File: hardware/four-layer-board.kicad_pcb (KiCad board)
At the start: 4 copper layers, 50 x 50 mm, 65 parts, among them J1 USB_B_Micro, J2 SWD Connector, J3 PWR, J4 Conn_01x06, J5 Conn_01x06, Q1 AO3401A, SW1 B3U-1000P, U1 STM32F103C8T6, U2 AMS1117-3.3, U3 USBLC6-2SC6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

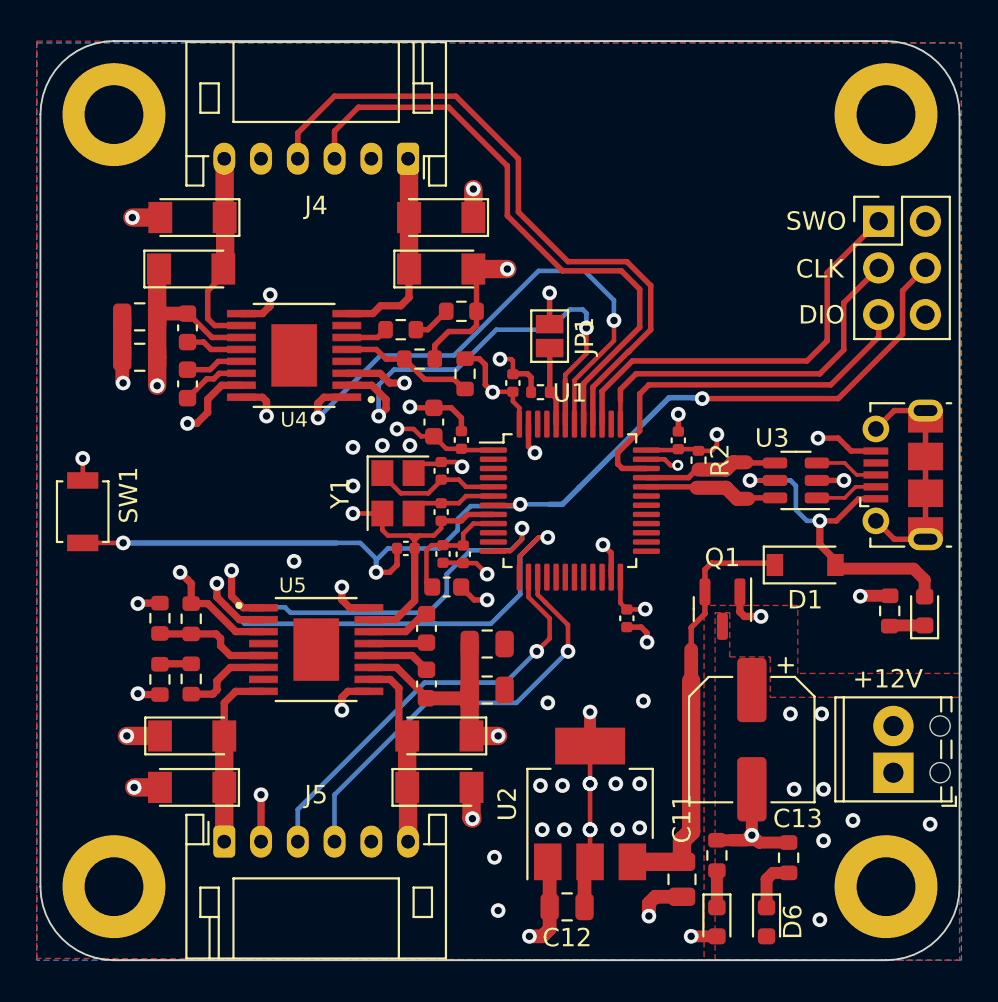
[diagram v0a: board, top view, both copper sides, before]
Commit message: Moved hardware to separate directory
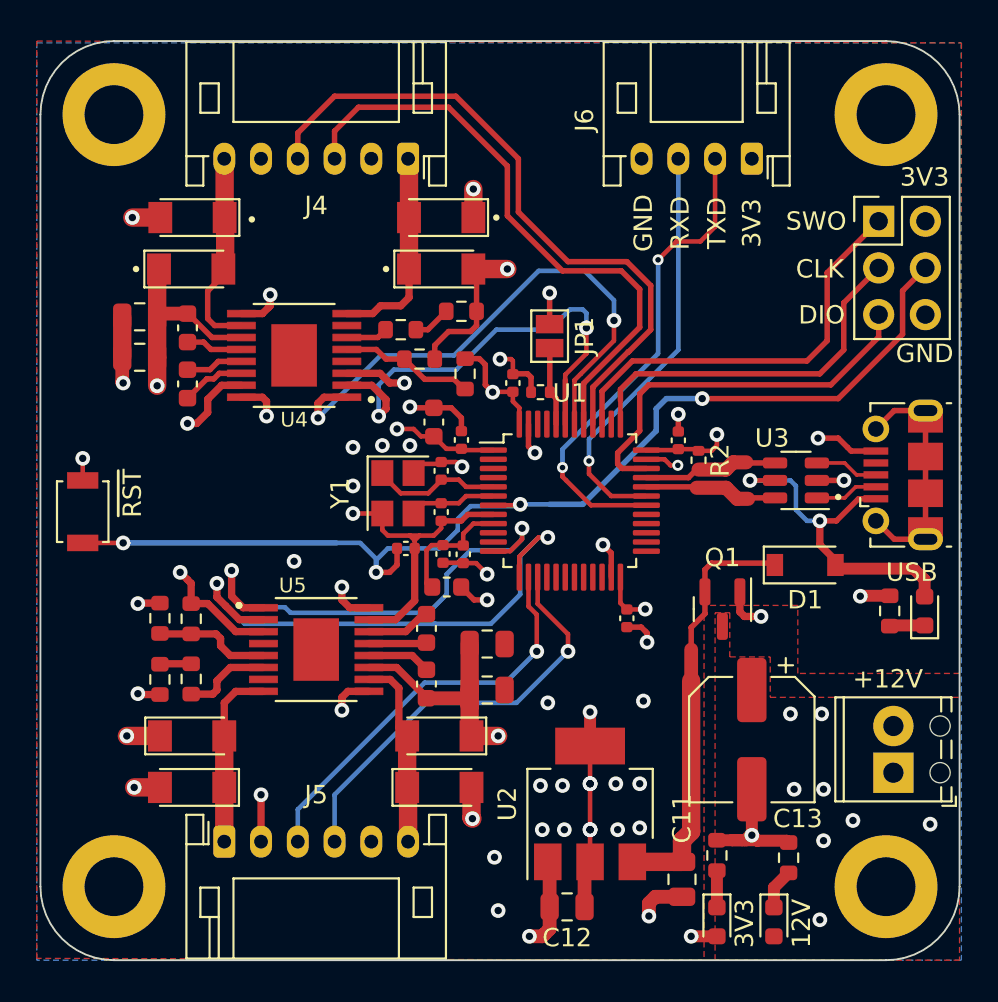
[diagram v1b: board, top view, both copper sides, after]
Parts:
- added J6: UART, Connector_JST:JST_PH_S4B-PH-K_1x04_P2.00mm_Horizontal, F.Cu at (168.7, 96.4)
- moved D6 0.40 mm to (169.9, 137.9)
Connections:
- U1 pad 30: unconnected-(U1-Pad30) -> /Microcontroller/USART1_TX
- U1 pad 31: unconnected-(U1-Pad31) -> /Microcontroller/USART1_RX
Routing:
- net /Microcontroller/USART1_TX: track 0.00 -> 26.7 mm, vias 0 -> 2
- net /Microcontroller/USART1_RX: track 0.00 -> 22.8 mm, vias 0 -> 1
- net Net-(D6-Pad1): track 2.87 -> 2.21 mm
- net /Microcontroller/NRST: track 59.7 -> 60.3 mm
- net /Microcontroller/M2_ENCA: track 23.1 -> 22.5 mm
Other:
- board text added: "12V"
- board text added: "3V3"
- board text added: "GND"
- board text added: "RXD"
- board text added: "TXD"
- board text added: "USB"
- board text added: "~{RST}"

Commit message: Added LEDs and UART
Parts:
- added D13: orange, LED_SMD:LED_0603_1608Metric, F.Cu at (163.9, 102.3)
- added D14: green, LED_SMD:LED_0603_1608Metric, F.Cu at (167.5, 102.3)
- added R14: 10k, Resistor_SMD:R_0402_1005Metric, F.Cu at (135.5, 116.8)
- added R15: 1k5, Resistor_SMD:R_0402_1005Metric, F.Cu at (164.1, 105.0)
- added R16: 1k5, Resistor_SMD:R_0402_1005Metric, F.Cu at (168.4, 104.9)
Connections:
- J6 pad 2: /Microcontroller/USART1_TX -> /Microcontroller/USART1_RX
- J6 pad 3: /Microcontroller/USART1_RX -> /Microcontroller/USART1_TX
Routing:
- net +3.3V: track 67.3 -> 70.5 mm, vias 25 -> 26
- net GND: track 91.6 -> 94.4 mm, vias 37 -> 39
- net Net-(D13-Pad1): track 0.00 -> 2.60 mm
- net Net-(D14-Pad1): track 0.00 -> 2.14 mm
- net /Microcontroller/USART1_RX: track 22.8 -> 24.0 mm, vias 1 -> 2
- net VBUS: track 19.2 -> 20.1 mm, vias 2 -> 0
- net /Microcontroller/M1_ENCA: track 32.9 -> 32.2 mm
- net /Microcontroller/M1_ENCB: track 36.2 -> 35.6 mm
- added copper zone on F.Cu, net +3.3V

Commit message: Added BOOT1 jumper
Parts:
- added JP2: Boot Jumper, Jumper:SolderJumper-2_P1.3mm_Open_Pad1.0x1.5mm, B.Cu at (163.6, 123.7)
- added R17: 10k, Resistor_SMD:R_0402_1005Metric, F.Cu at (160.0, 121.5)
- added REF**: OSHW-Logo2_7.3x6mm_SilkScreen, Symbol:OSHW-Logo2_7.3x6mm_SilkScreen, F.Cu at (142.9, 114.6)
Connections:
- U1 pad 20: unconnected-(U1-Pad20) -> /Microcontroller/BOOT1
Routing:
- net /Microcontroller/BOOT1: track 0.00 -> 7.15 mm, vias 0 -> 1
- net +3.3V: track 70.5 -> 74.4 mm
- net GND: track 94.4 -> 92.7 mm, vias 39 -> 38
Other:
- board text added: "JLCJLCJLCJLC"
- board text added: "POSIT Motor Control rev. A"
- board text added: "Sampreet Sarkar"

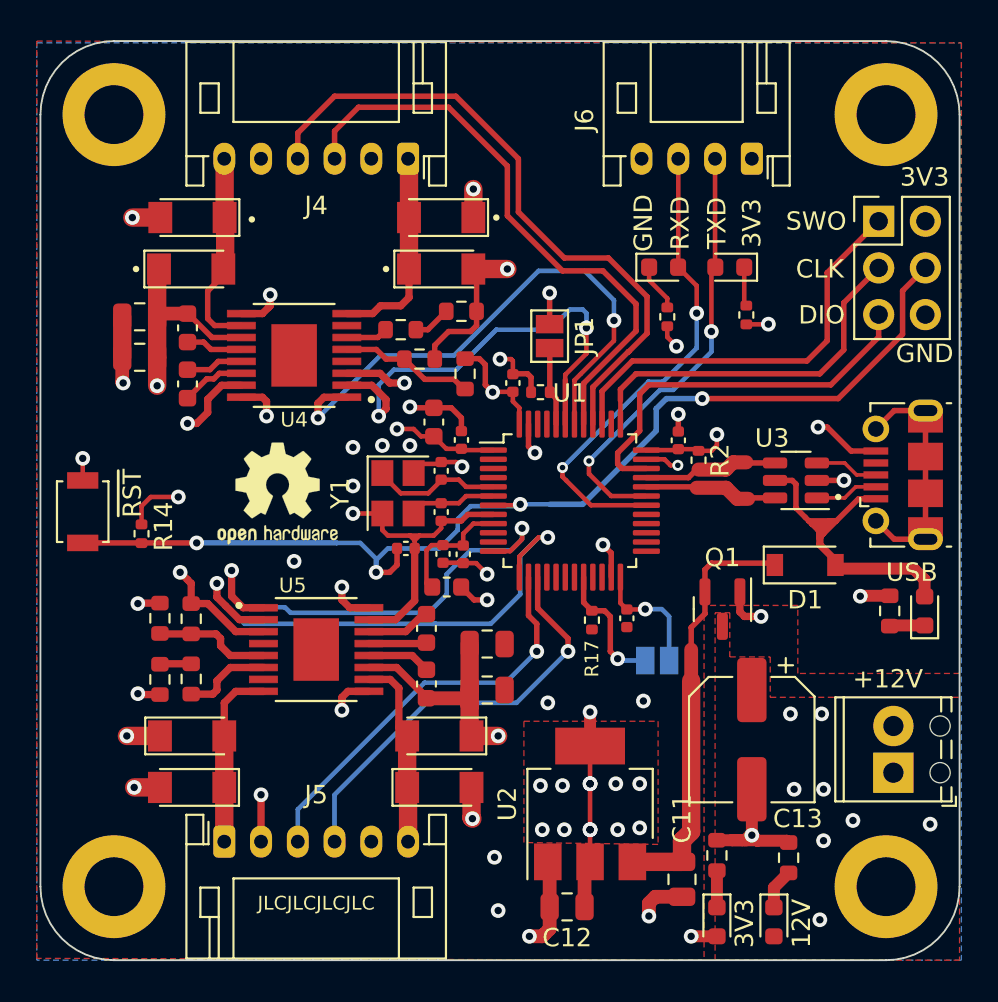
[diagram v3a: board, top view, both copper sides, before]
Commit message: Added status LED and silkscreen
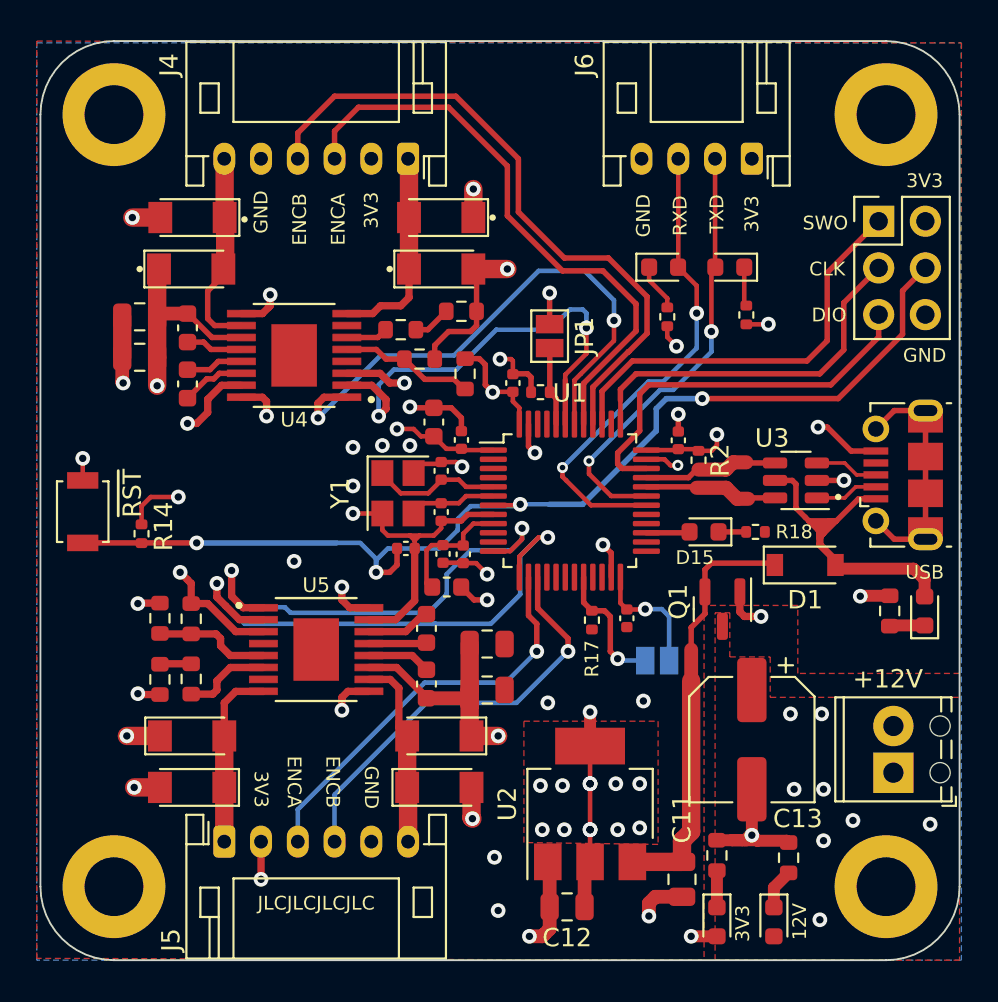
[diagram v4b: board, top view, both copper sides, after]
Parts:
- removed REF**: OSHW-Logo2_7.3x6mm_SilkScreen, Symbol:OSHW-Logo2_7.3x6mm_SilkScreen
- added D15: orange, LED_SMD:LED_0603_1608Metric, F.Cu at (166.1, 116.7)
- added R18: 1k5, Resistor_SMD:R_0402_1005Metric, F.Cu at (168.9, 116.7)
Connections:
- U1 pad 27: unconnected-(U1-Pad27) -> Net-(U1-Pad27)
- U4 pad 17: (no net) -> GND
- U5 pad 17: (no net) -> GND
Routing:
- net Net-(U1-Pad27): track 0.00 -> 2.37 mm
- net Net-(D15-Pad1): track 0.00 -> 1.50 mm
- net +3.3V: track 74.4 -> 73.9 mm
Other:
- board text added: "ENCA"
- board text added: "ENCB"

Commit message: Minor changes, added 100n cap
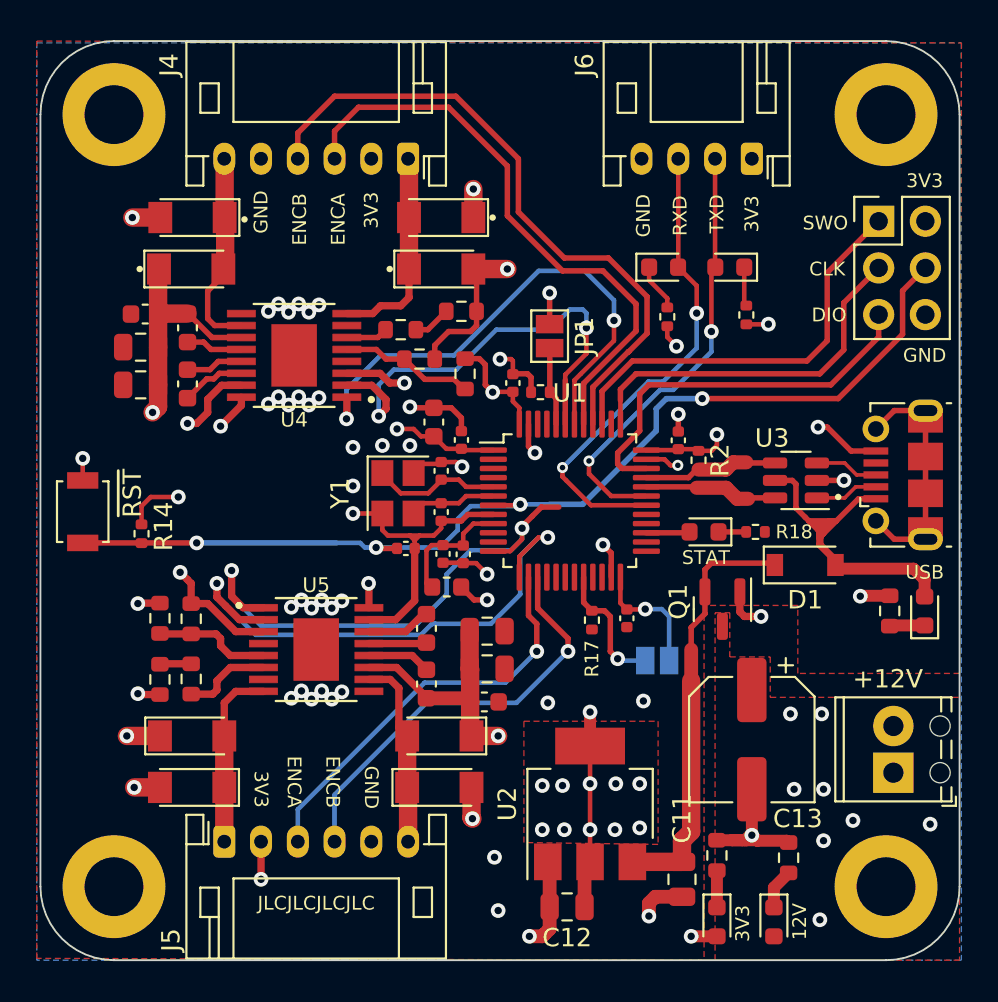
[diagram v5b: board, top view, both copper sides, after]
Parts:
- added C22: 100n, Capacitor_SMD:C_0603_1608Metric, F.Cu at (135.7, 104.8)
- added C23: 100n, Capacitor_SMD:C_0603_1608Metric, F.Cu at (154.2, 126.0)
- moved C16 1.65 mm to (135.4, 106.7)
- moved C17 1.50 mm to (135.4, 108.7)
- moved C21 1.15 mm to (154.3, 124.2)
- moved C20 0.70 mm to (154.3, 122.1)
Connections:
- net /Motor Driver/M2_IN1 renamed /Microcontroller/M2_IN1
- net /Motor Driver/M2_IN2 renamed /Microcontroller/M2_IN2
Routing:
- net GND: track 92.7 -> 84.5 mm, vias 38 -> 58
- net /Microcontroller/M2_IN1: track 26.3 -> 29.4 mm
- net /Microcontroller/NRST: track 60.7 -> 57.7 mm
- net +12V: track 28.7 -> 31.1 mm
- net /Microcontroller/M1_IN1: track 30.2 -> 28.3 mm
- net +3.3V: track 73.9 -> 72.6 mm, vias 26 -> 24
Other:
- board text added: "STAT"

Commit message: Updated hardware design, added TagConnect Probe and Battery Voltage Measurement
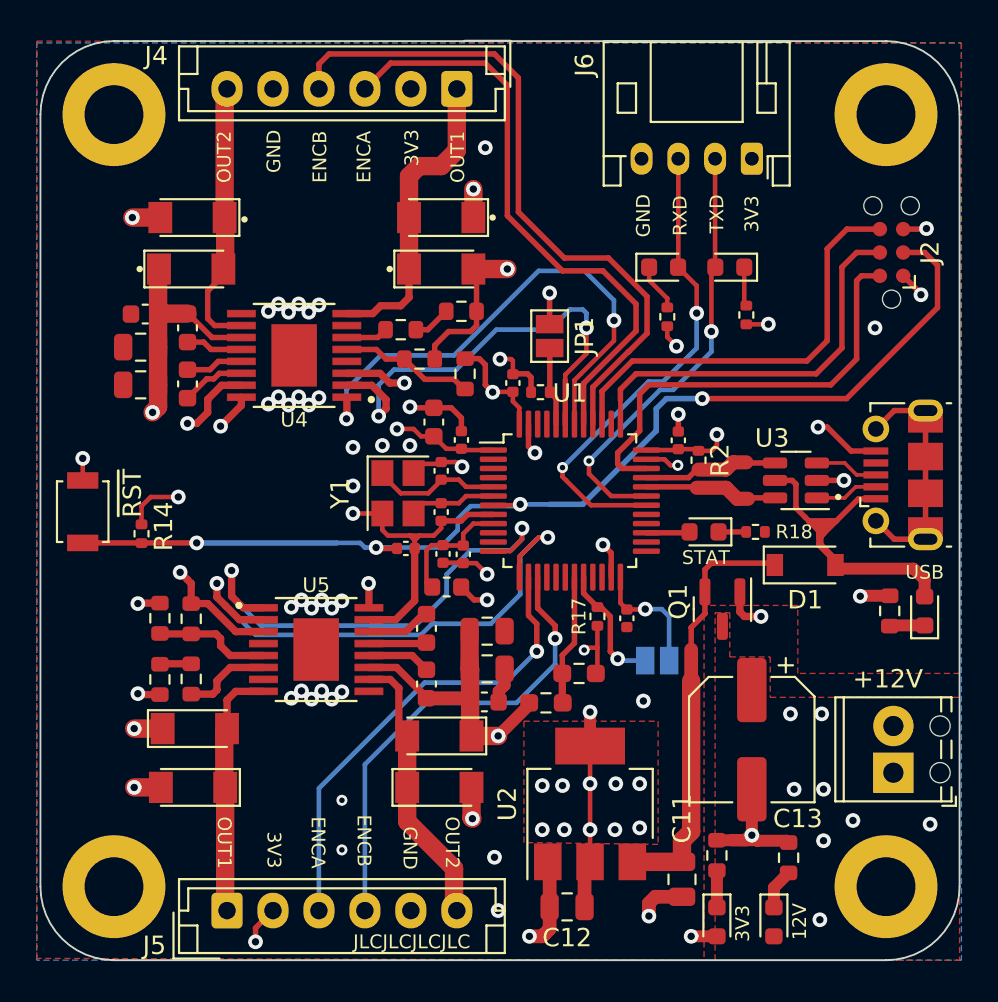
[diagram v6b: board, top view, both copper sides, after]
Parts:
- added R19: 1k5, Resistor_SMD:R_0603_1608Metric_Pad0.98x0.95mm_HandSolder, F.Cu at (157.5, 126.0)
- added R20: 1k5, Resistor_SMD:R_0603_1608Metric_Pad0.98x0.95mm_HandSolder, F.Cu at (159.3, 124.4)
- J2: value SWD Connector -> Conn_ARM_SWD_TagConnect_TC2030-NL; footprint Connector_PinHeader_2.54mm:PinHeader_2x03_P2.54mm_Vertical -> Connector:Tag-Connect_TC2030-IDC-NL_2x03_P1.27mm_Vertical
- J4, J5: value Conn_01x06 -> JST-EH_B6B; footprint Connector_JST:JST_PH_S6B-PH-K_1x06_P2.00mm_Horizontal -> Connector_JST:JST_EH_B6B-EH-A_1x06_P2.50mm_Vertical
- moved J4 4.63 mm to (152.7, 92.6)
- moved J5 3.75 mm to (140.2, 137.3)
- moved J2 1.84 mm to (176.3, 101.5), turned to 90 degrees
- moved D8 0.43 mm to (138.4, 127.4)
- moved R17 0.36 mm to (160.3, 121.3)
- moved D9 0.05 mm to (138.3, 130.6)
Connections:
- J2 pad 1: /Microcontroller/SWO -> +3.3V
- J2 pad 2: +3.3V -> /Microcontroller/SWDIO
- J2 pad 3: /Microcontroller/SWCLK -> /Microcontroller/NRST
- J2 pad 4: /Microcontroller/NRST -> /Microcontroller/SWCLK
- J2 pad 5: /Microcontroller/SWDIO -> GND
- J2 pad 6: GND -> /Microcontroller/SWO
- U1 pad 19: unconnected-(U1-Pad19) -> /Microcontroller/BATT_STAT
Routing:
- net +3.3V: track 72.6 -> 58.9 mm, vias 24 -> 25
- net /Microcontroller/BATT_STAT: track 0.00 -> 7.12 mm
- net GND: track 84.5 -> 91.1 mm, vias 58 -> 63
- net /Motor Driver/M1_OUT1: track 11.3 -> 16.9 mm
- net /Motor Driver/M2_OUT2: track 10.4 -> 15.2 mm
- net /Motor Driver/M1_OUT2: track 11.1 -> 14.9 mm
- net /Motor Driver/M2_OUT1: track 9.94 -> 13.8 mm
- net /Microcontroller/M2_ENCA: track 22.5 -> 25.8 mm
- net /Microcontroller/NRST: track 57.7 -> 60.6 mm
- net /Microcontroller/SWDIO: track 21.5 -> 24.2 mm
- net /Microcontroller/M2_ENCB: track 23.2 -> 25.7 mm
- net /Microcontroller/M2_IN1: track 29.4 -> 27.0 mm
- net +12V: track 31.1 -> 33.1 mm
- net /Microcontroller/M1_ENCB: track 35.6 -> 37.3 mm
- net /Microcontroller/SWCLK: track 20.7 -> 21.7 mm
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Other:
- board text added: "OUT1"
- board text added: "OUT2"
- board text removed: "CLK"
- board text removed: "DIO"
- board text removed: "SWO"

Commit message: Updated design, ready to generate production files
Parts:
- C10: value 0u1 -> 1u
- R19: value 1k5 -> 47k
- R20: value 1k5 -> 10k
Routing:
- net GND: track 91.1 -> 92.4 mm

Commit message: Cleaned up debug firmware
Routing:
- net GND: vias 63 -> 73
